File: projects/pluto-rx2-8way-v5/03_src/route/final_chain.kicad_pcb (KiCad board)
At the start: 4 copper layers, 90 x 65 mm, 36 parts, among them J1 C5184243, J10 C429844, J11 C2932107, J2 C429844, J3 C429844, J4 C429844, J5 C429844, J6 C429844, J7 C429844, J8 C429844, J9 C429844, U1 C5121458, U2 C5452432, U3 C2866134, U4 C1972959

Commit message: feat(pluto-v5): promote guarded control routing
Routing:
- net 3V3: track 0.00 -> 92.8 mm, vias 0 -> 1
- net RF_ANT5: track 0.00 -> 36.6 mm
- net RF_ANT4: track 0.00 -> 36.6 mm
- net RF_ANT2: track 0.00 -> 35.1 mm
- net RF_ANT7: track 0.00 -> 35.1 mm
- net GND: track 0.00 -> 32.8 mm, vias 9 -> 32
- net SWDIO: track 0.00 -> 32.7 mm, vias 0 -> 2
- net SWCLK: track 0.00 -> 31.6 mm
- net RF_ANT6: track 0.00 -> 31.5 mm
- net RF_ANT3: track 0.00 -> 31.5 mm
- net SW_V1: track 0.00 -> 29.7 mm, vias 0 -> 3
- net VBUS_RAW: track 0.00 -> 29.4 mm
- net NRST: track 0.00 -> 27.7 mm, vias 0 -> 5
- net RF_ANT8: track 0.00 -> 22.4 mm
- net RF_ANT1: track 0.00 -> 22.4 mm
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
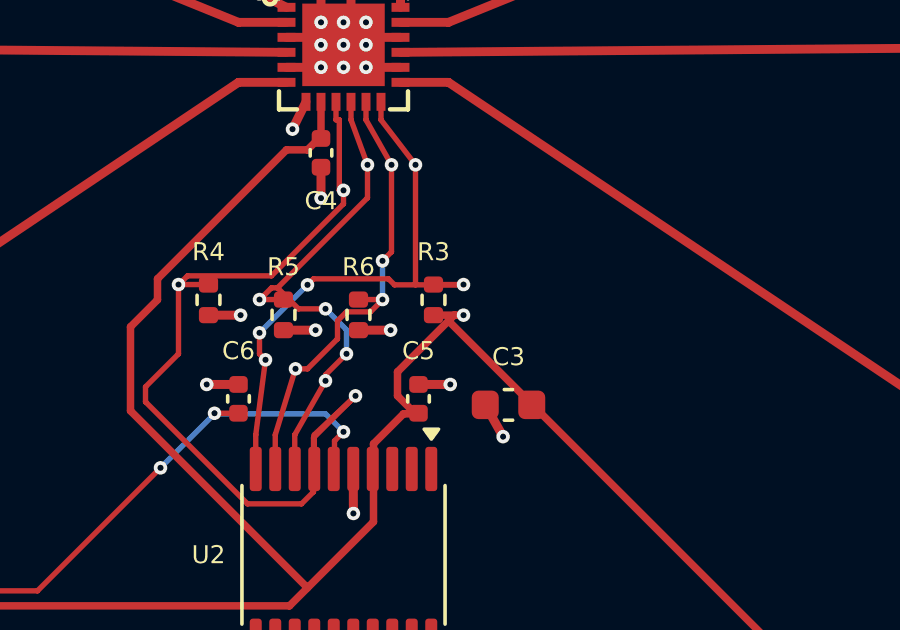
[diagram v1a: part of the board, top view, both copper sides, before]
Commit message: feat(pluto-v5): complete post-stitch validation
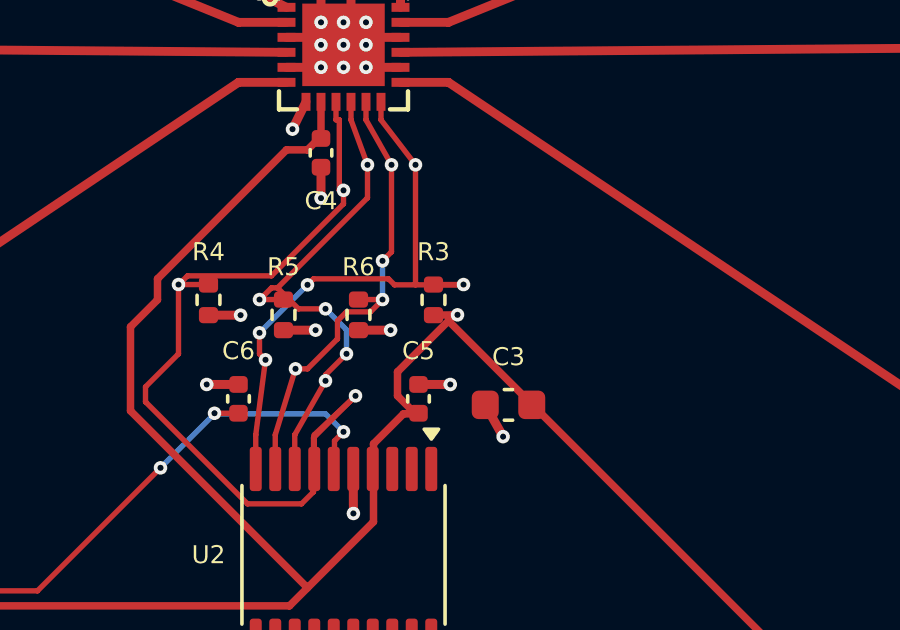
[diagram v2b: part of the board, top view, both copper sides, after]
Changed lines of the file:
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@@
 	(segment
 		(start 68 57.01)
-		(end 69 57.01)
+		(end 68.8 57)
 		(width 0.25)
 		(layer "F.Cu")
@@
 	)
 	(via
-		(at 69 57.01)
+		(at 68.8 57)
 		(size 0.45)
 		(drill 0.2)

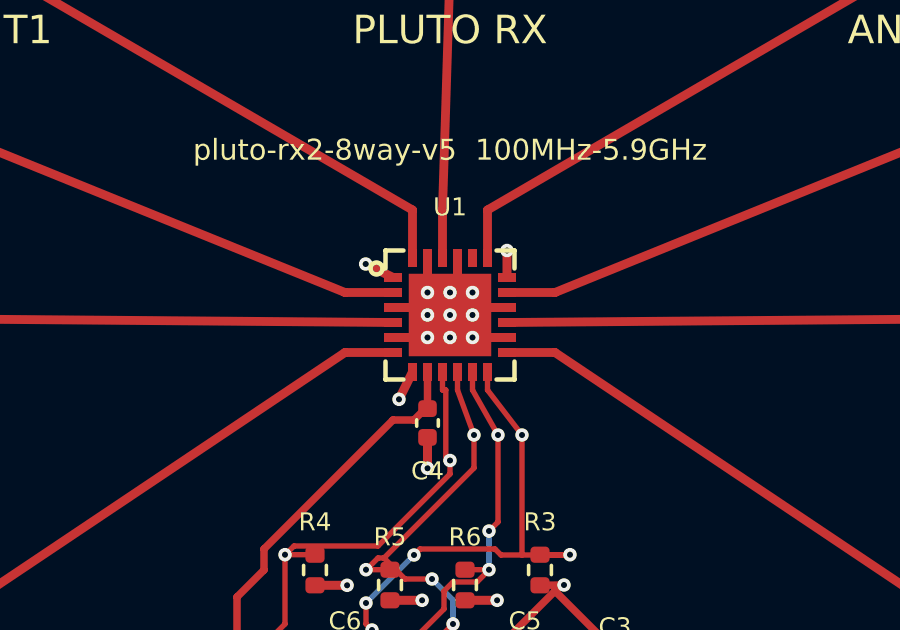
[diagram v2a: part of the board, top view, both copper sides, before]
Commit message: fix(pluto-v5): reject undeclared via-in-pad
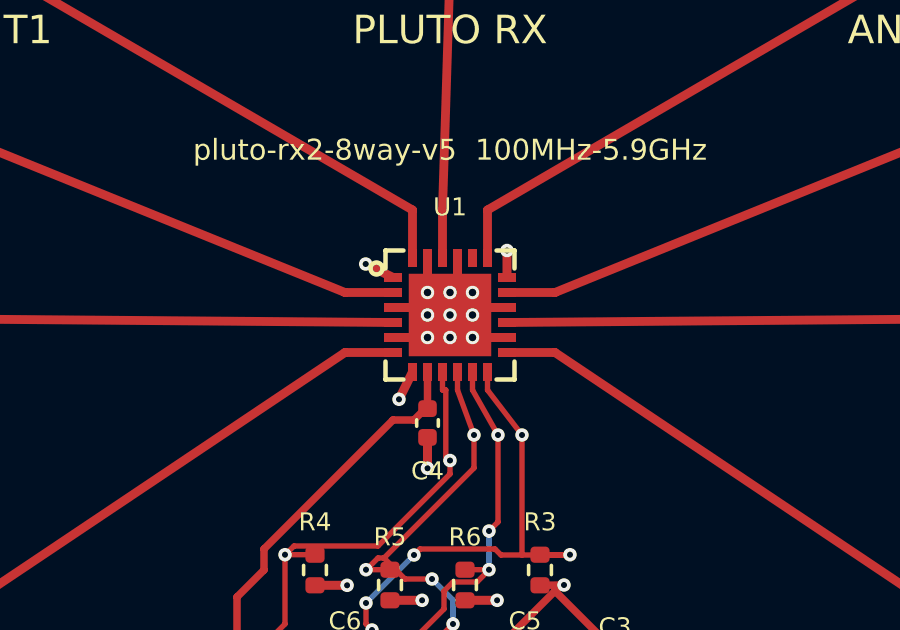
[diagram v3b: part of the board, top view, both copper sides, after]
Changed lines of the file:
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@@
 		(at 65.75 48)
 		(size 0.45)
-		(drill 0.2)
+		(drill 0.25)
 		(layers "F.Cu" "B.Cu")
 		(capping yes)
@@
 		(at 65 48)
 		(size 0.45)
-		(drill 0.2)
+		(drill 0.25)
 		(layers "F.Cu" "B.Cu")
 		(capping yes)
@@
 		(at 64.25 47.25)
 		(size 0.45)
-		(drill 0.2)
+		(drill 0.25)
 		(layers "F.Cu" "B.Cu")
 		(capping yes)
@@
 		(at 64.25 48)
 		(size 0.45)
-		(drill 0.2)
+		(drill 0.25)
 		(layers "F.Cu" "B.Cu")
 		(capping yes)
@@
 		(at 65.75 47.25)
 		(size 0.45)
-		(drill 0.2)
+		(drill 0.25)
 		(layers "F.Cu" "B.Cu")
 		(capping yes)
@@
 		(at 65 47.25)
 		(size 0.45)
-		(drill 0.2)
+		(drill 0.25)
 		(layers "F.Cu" "B.Cu")
 		(capping yes)
@@
 		(at 65 48.75)
 		(size 0.45)
-		(drill 0.2)
+		(drill 0.25)
 		(layers "F.Cu" "B.Cu")
 		(capping yes)
@@
 		(at 64.25 48.75)
 		(size 0.45)
-		(drill 0.2)
+		(drill 0.25)
 		(layers "F.Cu" "B.Cu")
 		(capping yes)
@@
 		(at 65.75 48.75)
 		(size 0.45)
-		(drill 0.2)
+		(drill 0.25)
 		(layers "F.Cu" "B.Cu")
 		(capping yes)

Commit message: Add Pluto bench power and correct SMA renders
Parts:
- added J12: C225477, Connector_PinHeader_2.54mm:PinHeader_1x02_P2.54mm_Vertical, F.Cu at (54.0, 77.0)
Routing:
- net VBUS_RAW: track 29.4 -> 35.1 mm
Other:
- board text added: "+5V"
- board text added: "BENCH 5V"
- board text added: "FUSE"
- board text added: "GND"
- board text added: "J12"
- board text added: "POWER ONLY"
- board text added: "USB OR J12 - NOT BOTH"
- board text added: "USB-C"
- board text removed: "USB-C POWER ONLY"

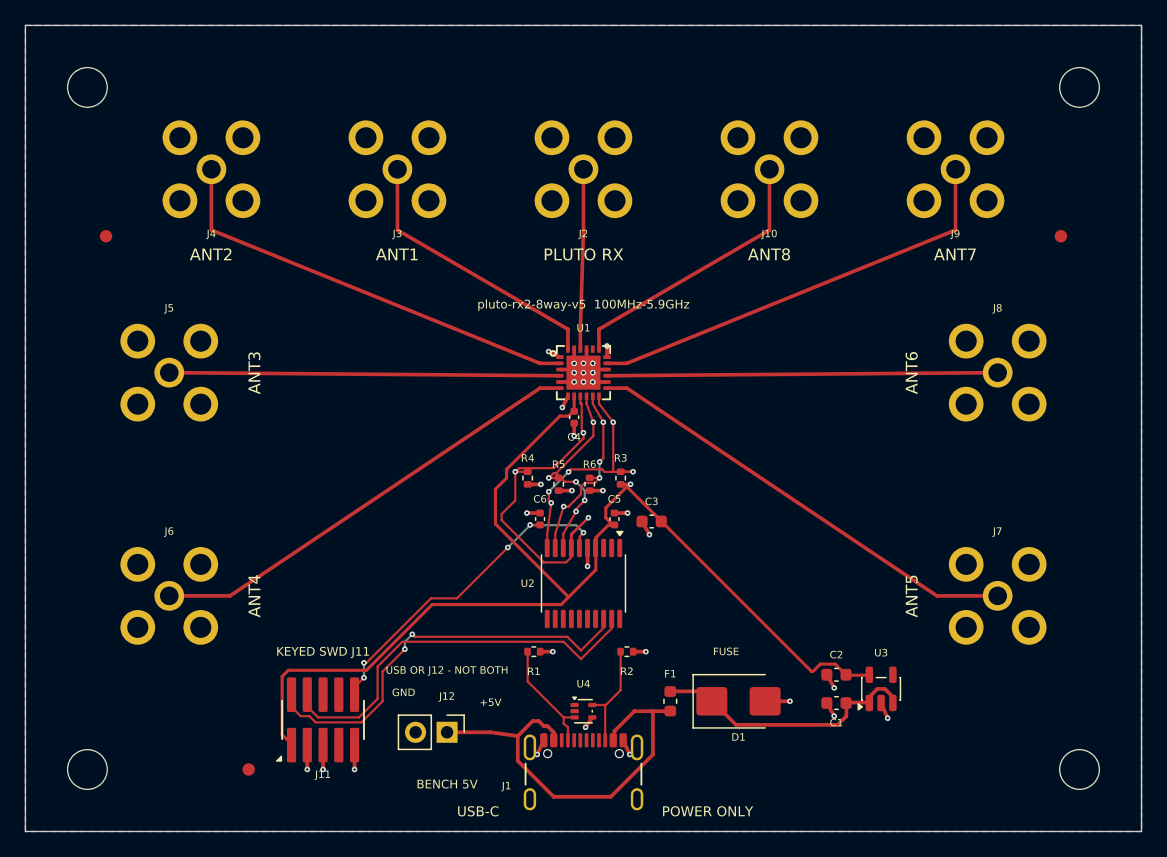
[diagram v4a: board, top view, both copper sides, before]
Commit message: pluto: integrate bench power, rounded RF, and model registration
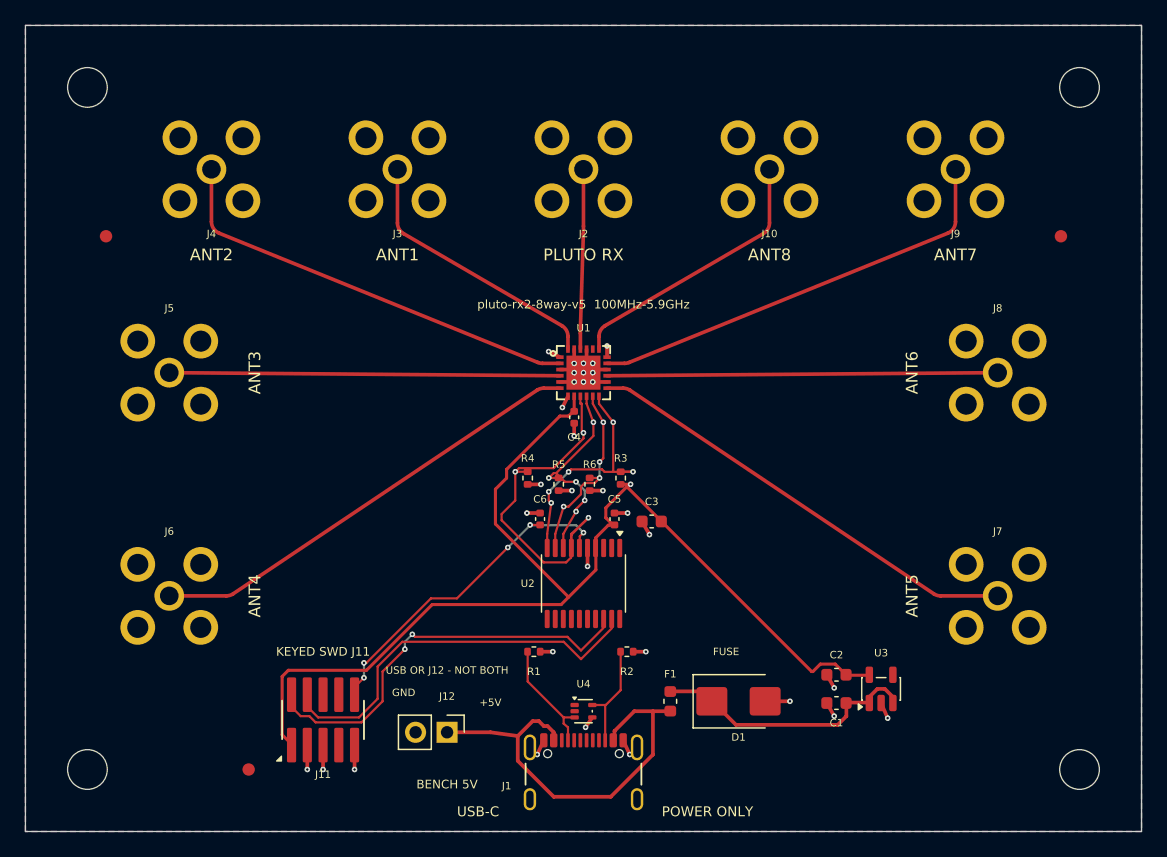
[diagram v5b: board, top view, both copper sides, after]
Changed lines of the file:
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@@
 	)
 	(segment
-		(start 61.5 47.25)
-		(end 35 36.5)
+		(start 35 35.827)
+		(end 35 31.6)
 		(width 0.295)
 		(layer "F.Cu")
@@
 	)
 	(segment
+		(start 61.319 47.177)
+		(end 35.624 36.753)
+		(width 0.295)
+		(layer "F.Cu")
+		(net "RF_ANT2")
+	)
+	(segment
 		(start 63.1 47.25)
-		(end 61.5 47.25)
+		(end 61.695 47.25)
 		(width 0.295)
 		(layer "F.Cu")
 		(net "RF_ANT2")
 	)
-	(segment
-		(start 35 36.5)
-		(end 35 31.6)
+	(arc
+		(start 61.695 47.25)
+		(mid 61.504 47.232)
+		(end 61.319 47.177)
+		(width 0.295)
+		(layer "F.Cu")
+		(net "RF_ANT2")
+	)
+	(arc
+		(start 35.624 36.753)
+		(mid 35.171 36.385)
+		(end 35 35.827)
 		(width 0.295)
 		(layer "F.Cu")
@@
 	)
 	(segment
+		(start 36.196 66)
+		(end 31.6 66)
+		(width 0.295)
+		(layer "F.Cu")
+		(net "RF_ANT4")
+	)
+	(segment
 		(start 63.1 49.25)
-		(end 61.5 49.25)
+		(end 61.804 49.25)
 		(width 0.295)
 		(layer "F.Cu")
@@
 	)
 	(segment
-		(start 61.5 49.25)
-		(end 36.5 66)
+		(start 61.247 49.419)
+		(end 36.753 65.831)
 		(width 0.295)
 		(layer "F.Cu")
 		(net "RF_ANT4")
 	)
-	(segment
-		(start 36.5 66)
-		(end 31.6 66)
+	(arc
+		(start 36.753 65.831)
+		(mid 36.487 65.956999)
+		(end 36.196 66)
+		(width 0.295)
+		(layer "F.Cu")
+		(net "RF_ANT4")
+	)
+	(arc
+		(start 61.804 49.25)
+		(mid 61.513 49.293)
+		(end 61.247 49.419)
 		(width 0.295)
 		(layer "F.Cu")
@@
 	)
 	(segment
-		(start 68.5 49.25)
-		(end 93.5 66)
+		(start 93.804 66)
+		(end 98.4 66)
 		(width 0.295)
 		(layer "F.Cu")
@@
 	)
 	(segment
-		(start 93.5 66)
-		(end 98.4 66)
+		(start 68.753 49.419)
+		(end 93.247 65.831)
 		(width 0.295)
 		(layer "F.Cu")
@@
 	(segment
 		(start 66.9 49.25)
-		(end 68.5 49.25)
+		(end 68.196 49.25)
+		(width 0.295)
+		(layer "F.Cu")
+		(net "RF_ANT5")
+	)
+	(arc
+		(start 68.196 49.25)
+		(mid 68.487 49.293)
+		(end 68.753 49.419)
+		(width 0.295)
+		(layer "F.Cu")
+		(net "RF_ANT5")
+	)
+	(arc
+		(start 93.247 65.831)
+		(mid 93.513 65.956999)
+		(end 93.804 66)
 		(width 0.295)
 		(layer "F.Cu")
@@
 	)
 	(segment
-		(start 68.5 47.25)
-		(end 95 36.5)
+		(start 95 35.827)
+		(end 95 31.6)
 		(width 0.295)
 		(layer "F.Cu")
@@
 	)
 	(segment
-		(start 95 36.5)
-		(end 95 31.6)
+		(start 66.9 47.25)
+		(end 68.305 47.25)
 		(width 0.295)
 		(layer "F.Cu")
@@
 	)
 	(segment
-		(start 66.9 47.25)
-		(end 68.5 47.25)
+		(start 68.681 47.177)
+		(end 94.376 36.753)
 		(width 0.295)
 		(layer "F.Cu")
 		(net "RF_ANT7")
 	)
+	(arc
+		(start 68.305 47.25)
+		(mid 68.496 47.232)
+		(end 68.681 47.177)
+		(width 0.295)
+		(layer "F.Cu")
+		(net "RF_ANT7")
+	)
+	(arc
+		(start 94.376 36.753)
+		(mid 94.829 36.385)
+		(end 95 35.827)
+		(width 0.295)
+		(layer "F.Cu")
+		(net "RF_ANT7")
+	)
+	(segment
+		(start 66.747 44.211)
+		(end 79.503 36.789)
+		(width 0.295)
+		(layer "F.Cu")
+		(net "RF_ANT8")
+	)
+	(segment
+		(start 80 35.925)
+		(end 80 31.6)
+		(width 0.295)
+		(layer "F.Cu")
+		(net "RF_ANT8")
+	)
 	(segment
 		(start 66.25 46.1)
-		(end 66.25 44.5)
+		(end 66.25 45.075)
 		(width 0.295)
 		(layer "F.Cu")
 		(net "RF_ANT8")
 	)
-	(segment
-		(start 80 36.5)
-		(end 80 31.6)
+	(arc
+		(start 79.503 36.789)
+		(mid 79.867 36.423)
+		(end 80 35.925)
 		(width 0.295)
 		(layer "F.Cu")
 		(net "RF_ANT8")
 	)
-	(segment
-		(start 66.25 44.5)
-		(end 80 36.5)
+	(arc
+		(start 66.25 45.075)
+		(mid 66.382999 44.577)
+		(end 66.747 44.211)
 		(width 0.295)
 		(layer "F.Cu")
@@
 	)
 	(segment
+		(start 64.76 44.188)
+		(end 64.989999 36.812)
+		(width 0.295)
+		(layer "F.Cu")
+		(net "RF_COMMON")
+	)
+	(segment
+		(start 65 36.188)
+		(end 65 31.6)
+		(width 0.295)
+		(layer "F.Cu")
+		(net "RF_COMMON")
+	)
+	(segment
 		(start 64.75 46.1)
-		(end 64.75 44.5)
+		(end 64.75 44.812)
 		(width 0.295)
 		(layer "F.Cu")
 		(net "RF_COMMON")
 	)
-	(segment
-		(start 65 36.5)
-		(end 65 31.6)
+	(arc
+		(start 64.989999 36.812)
+		(mid 64.998 36.5)
+		(end 65 36.188)
 		(width 0.295)
 		(layer "F.Cu")
 		(net "RF_COMMON")
 	)
-	(segment
-		(start 64.75 44.5)
-		(end 65 36.5)
+	(arc
+		(start 64.75 44.812)
+		(mid 64.751999 44.5)
+		(end 64.76 44.188)
 		(width 0.295)
 		(layer "F.Cu")
@@
 	(segment
 		(start 63.75 46.1)
-		(end 63.75 44.5)
+		(end 63.75 45.075)
 		(width 0.295)
 		(layer "F.Cu")
@@
 	)
 	(segment
-		(start 50 36.5)
+		(start 50 35.925)
 		(end 50 31.6)
 		(width 0.295)
@@
 	)
 	(segment
-		(start 63.75 44.5)
-		(end 50 36.5)
-		(width 0.295)
-		(layer "F.Cu")
+		(start 63.253 44.211)
+		(end 50.497 36.789)
+		(width 0.295)
+		(layer "F.Cu")
+		(net "RF_ANT1")
+	)
+	(arc
+		(start 50.497 36.789)
+		(mid 50.133 36.423)
+		(end 50 35.925)
+		(width 0.295)
+		(layer "F.Cu")
+		(net "RF_ANT1")
+	)
+	(arc
+		(start 63.75 45.075)
+		(mid 63.617 44.577)
+		(end 63.253 44.211)
+		(width 0.295)
+		(layer "F.Cu")
